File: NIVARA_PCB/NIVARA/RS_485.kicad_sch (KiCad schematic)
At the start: 1 part, among them U7 TD321D485H-A-LB

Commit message: ACTUALIZACION
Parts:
- added D3: SMBJ12CA, PCM_Diode_SMD_AKL:D_SMB_TVS, symbol PCM_Diode_TVS_AKL:SMBJ12CA
- added R34, R35: 47K, PCM_Resistor_SMD_AKL:R_0603_1608Metric, symbol PCM_Resistor_AKL:R_0603
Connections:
- net +3V3: now reaches U7.1 (VCC)
- net at U7.10 (RGND): now also R35.1
- net GND: now reaches U7.2 (GND)
- net TX: now reaches U7.3 (TXD)
- net RX: now reaches U7.4 (RXD)
- net at U7.7 (VO): now also R34.1
- net B: now reaches U7.8 (B)
- net B: now also R35.2
- net A: now reaches U7.9 (A)
- net A: now also R34.2
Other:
- moved on the sheet: U7

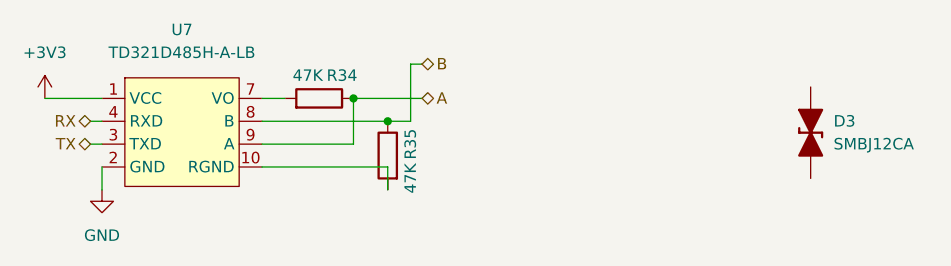
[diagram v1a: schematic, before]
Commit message: Se organizaron componentes en el area de PCB
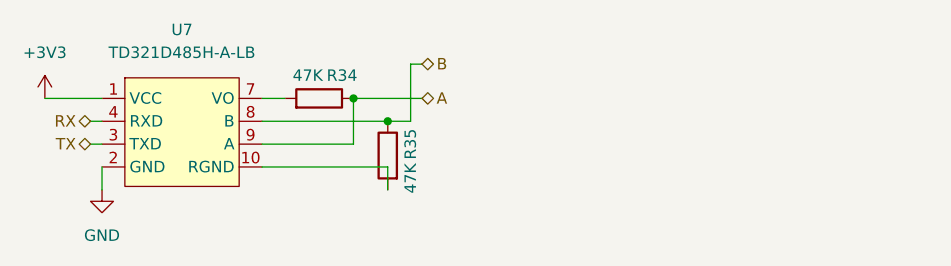
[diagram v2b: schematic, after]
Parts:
- removed D3: SMBJ12CA, PCM_Diode_SMD_AKL:D_SMB_TVS, symbol PCM_Diode_TVS_AKL:SMBJ12CA
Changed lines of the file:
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@@
-	)
-	(symbol
-		(lib_id "PCM_Diode_TVS_AKL:SMBJ12CA")
-		(at 204.47 82.55 90)
-		(unit 1)
-		(exclude_from_sim no)
-		(in_bom yes)
-		(on_board yes)
-		(dnp no)
-		(fields_autoplaced yes)
-		(property "Reference" "D3"
-			(at 207.01 81.2799 90)
-			(effects
-				(font
-					(size 1.27 1.27)
-				)
-				(justify right)
-			)
-		)
-		(property "Value" "SMBJ12CA"
-			(at 207.01 83.8199 90)
-			(effects
-				(font
-					(size 1.27 1.27)
-				)
-				(justify right)
-			)
-		)
-		(property "Footprint" "PCM_Diode_SMD_AKL:D_SMB_TVS"
-			(at 204.47 82.55 0)
-			(effects
-				(font
-					(size 1.27 1.27)
-				)
-				(hide yes)
-			)
-		)
-		(property "Datasheet" "https://www.tme.eu/Document/0b6222bec7e12d83185b51d73cb6a54d/SMBJ_ser.pdf"
-			(at 204.47 82.55 0)
-			(effects
-				(font
-					(size 1.27 1.27)
-				)
-				(hide yes)
-			)
-		)
-		(property "Description" "SMB Bidirectional TVS Diode, 12V, 600W, Alternate KiCAD Library"
-			(at 204.47 82.55 0)
-			(effects
-				(font
-					(size 1.27 1.27)
-				)
-				(hide yes)
-			)
-		)
-		(property "LCSC Part" "C46956407"
-			(at 204.47 82.55 0)
-			(effects
-				(font
-					(size 1.27 1.27)
-				)
-				(hide yes)
-			)
-		)
-		(property "PART NUMBERT" "SMBJ12CA"
-			(at 204.47 82.55 0)
-			(effects
-				(font
-					(size 1.27 1.27)
-				)
-				(hide yes)
-			)
-		)
-		(pin "1"
-		)
-		(pin "2"
-		)
-		(instances
-			(project ""
-				(path "/6298d7d5-28da-40bf-9586-24a8e5c02b82/7ff0dada-fc46-483c-91ad-b264be8c64cf/48a464e8-a5ed-43b1-9b1b-2c845d4bc246"
-					(reference "D3")
-					(unit 1)
-				)
-			)
-		)
 	)
 	(symbol
